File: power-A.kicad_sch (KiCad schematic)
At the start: 30 parts, among them J201 PCB Receptacle, J202 PCB Receptacle, J203 Conn_01x06, U201 AMS1117-ADJ_SOT223

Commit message: Ficup column name for JLCPCB/LCSC part no
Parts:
- C201: LCSC (none) -> C117040
- C203, C205: LCSC (none) -> C12891
- D201: LCSC (none) -> C78395
- D202, D203: LCSC (none) -> C12760
- D204, D205, D206: LCSC (none) -> C8598
- D207: LCSC (none) -> C2293
- R204, R210: LCSC (none) -> C25271
- U201: LCSC (none) -> C347224
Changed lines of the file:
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@@
+      (effects (font (size 1.27 1.27)) hide)
+    )
+    (property "LCSC" "C12760" (id 5) (at 68.58 93.98 0)
       (effects (font (size 1.27 1.27)) hide)
     )
@@
       (effects (font (size 1.27 1.27)) hide)
     )
+    (property "LCSC" "C25271" (id 5) (at 242.57 80.645 0)
+      (effects (font (size 1.27 1.27)) hide)
+    )
     (pin "1")
     (pin "2")
@@
       (effects (font (size 1.27 1.27)) hide)
     )
+    (property "LCSC" "C117040" (id 5) (at 139.7 91.44 0)
+      (effects (font (size 1.27 1.27)) hide)
+    )
     (pin "1")
     (pin "2")
@@
     )
     (property "JLCPCB" " C12891 " (id 4) (at 169.545 89.535 0)
+      (effects (font (size 1.27 1.27)) hide)
+    )
+    (property "LCSC" " C12891 " (id 5) (at 169.545 89.535 0)
       (effects (font (size 1.27 1.27)) hide)
     )
@@
       (effects (font (size 1.27 1.27)) hide)
     )
+    (property "LCSC" "C78395" (id 5) (at 60.325 91.44 0)
+      (effects (font (size 1.27 1.27)) hide)
+    )
     (pin "1")
     (pin "2")
@@
       (effects (font (size 1.27 1.27)) hide)
     )
+    (property "LCSC" "C347224" (id 5) (at 188.595 80.645 0)
+      (effects (font (size 1.27 1.27)) hide)
+    )
     (pin "1")
     (pin "2")
@@
     )
     (property "JLCPCB" "C8598 " (id 4) (at 190.5 138.43 0)
+      (effects (font (size 1.27 1.27)) hide)
+    )
+    (property "LCSC" "C8598 " (id 5) (at 190.5 138.43 0)
       (effects (font (size 1.27 1.27)) hide)
     )
@@
       (effects (font (size 1.27 1.27)) hide)
     )
+    (property "LCSC" "C25271" (id 5) (at 100.965 80.645 0)
+      (effects (font (size 1.27 1.27)) hide)
+    )
     (pin "1")
     (pin "2")
@@
     )
     (property "JLCPCB" "C12760" (id 4) (at 68.58 85.725 0)
+      (effects (font (size 1.27 1.27)) hide)
+    )
+    (property "LCSC" "C12760" (id 5) (at 68.58 85.725 0)
       (effects (font (size 1.27 1.27)) hide)
     )
@@
       (effects (font (size 1.27 1.27)) hide)
     )
+    (property "LCSC" "C8598 " (id 5) (at 190.5 128.27 0)
+      (effects (font (size 1.27 1.27)) hide)
+    )
     (pin "1")
     (pin "2")
@@
     )
     (property "JLCPCB" "C2293" (id 4) (at 255.27 92.075 0)
+      (effects (font (size 1.27 1.27)) hide)
+    )
+    (property "LCSC" "C2293" (id 5) (at 255.27 92.075 0)
       (effects (font (size 1.27 1.27)) hide)
     )
@@
       (effects (font (size 1.27 1.27)) hide)
     )
+    (property "LCSC" "C8598 " (id 5) (at 134.62 80.645 0)
+      (effects (font (size 1.27 1.27)) hide)
+    )
     (pin "1")
     (pin "2")
@@
       (effects (font (size 1.27 1.27)) hide)
     )
+    (property "LCSC" " C12891 " (id 5) (at 220.98 89.535 0)
+      (effects (font (size 1.27 1.27)) hide)
+    )

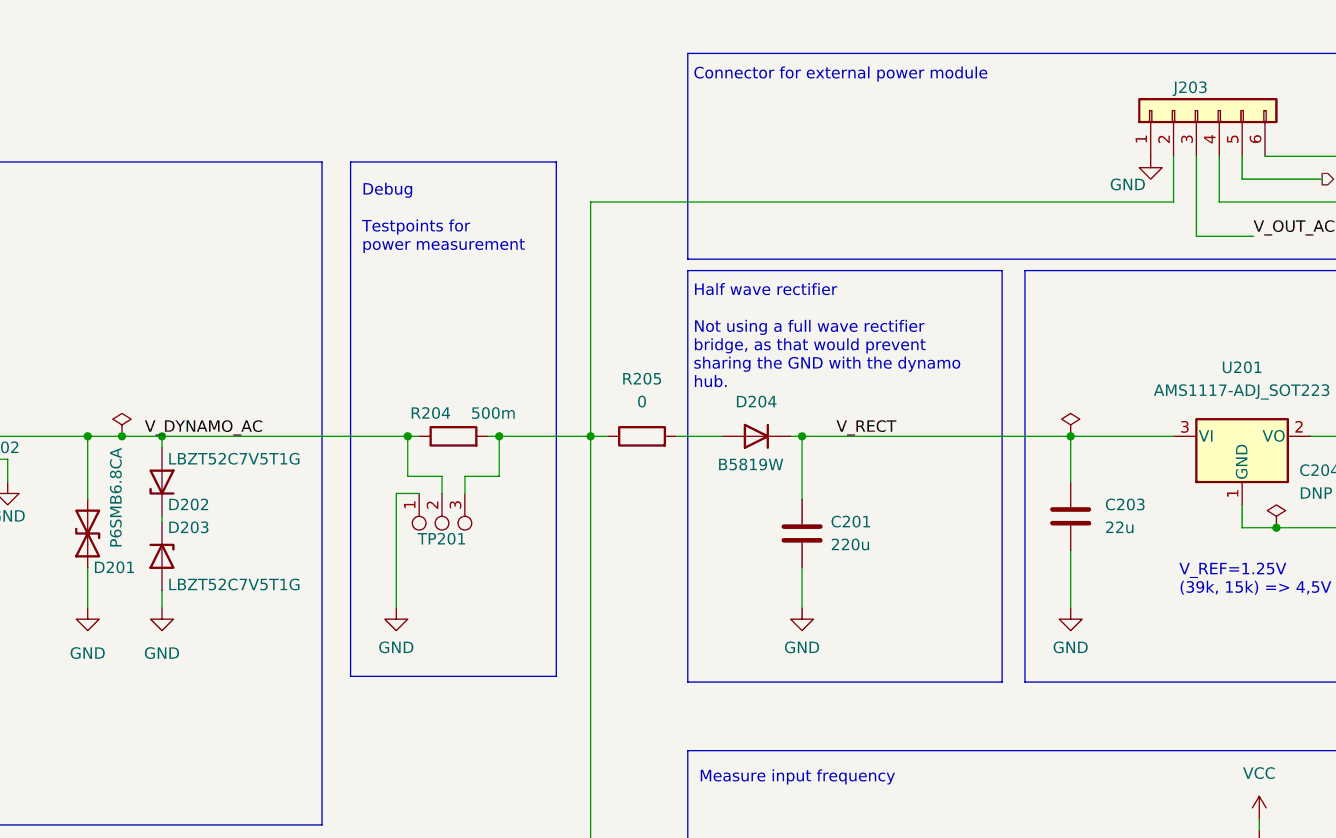
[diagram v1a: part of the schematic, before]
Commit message: move power module intput directly to V_DYNAMO_AC to ease routing
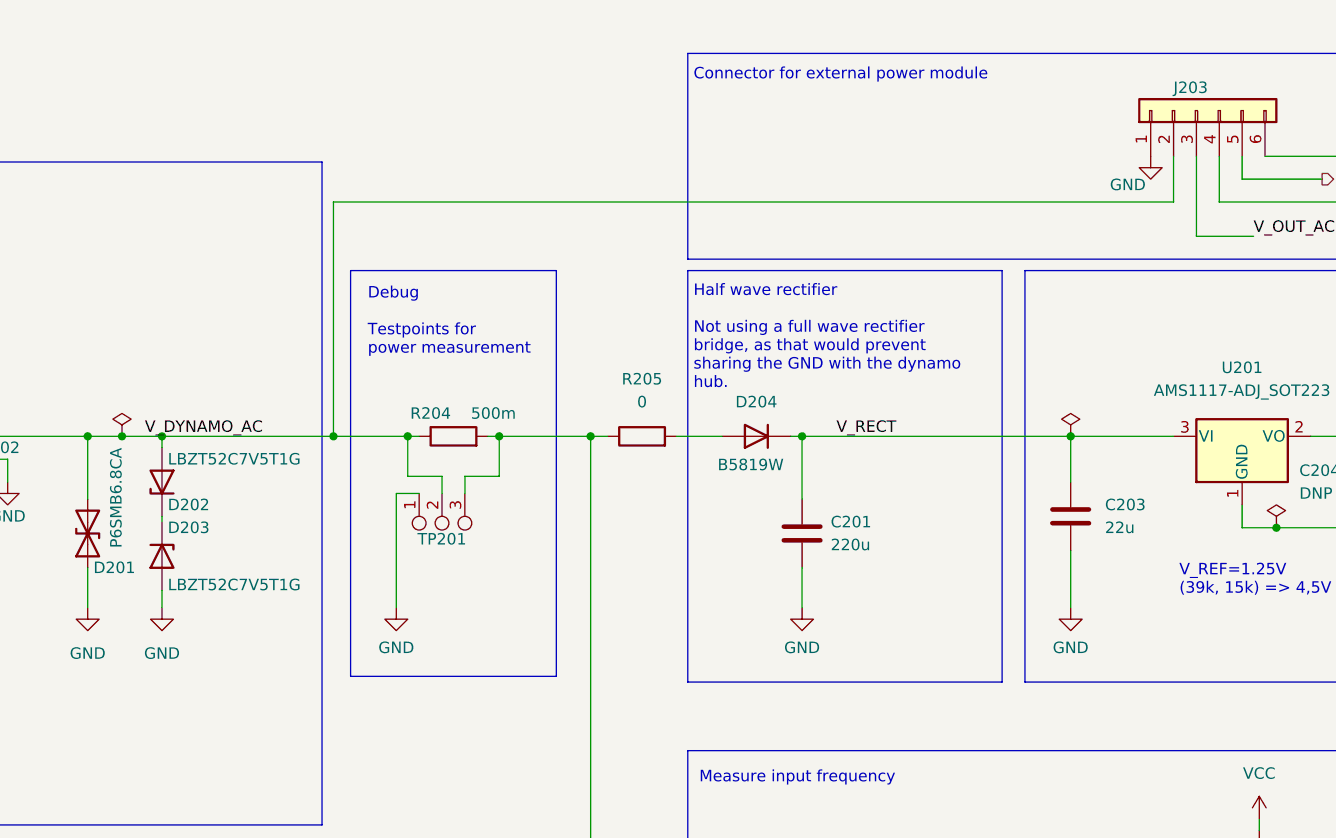
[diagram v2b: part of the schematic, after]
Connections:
- net V_DYNAMO_AC: now also J203.2 (Pin_2)
- net at R204.2, R205.1, R206.2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: no longer J203.2 (Pin_2)
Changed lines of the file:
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@@
     (comment 3 "CERN-OHL-S-2.0 https://spdx.org/licenses/CERN-OHL-S-2.0.html")
   )
+  (junction (at 87.63 80.645) (diameter 0) (color 0 0 0 0)
+  )
   (junction (at 95.885 80.645) (diameter 0) (color 0 0 0 0)
   )
@@
     (stroke (width 0) (type default) (color 0 0 0 0))
   )
-  (polyline (pts (xy 89.535 50.165) (xy 89.535 107.315))
+  (polyline (pts (xy 89.535 62.23) (xy 89.535 107.315))
     (stroke (width 0) (type default) (color 0 0 0 0))
   )
@@
     (stroke (width 0) (type default) (color 0 0 0 0))
   )
-  (polyline (pts (xy 112.395 50.165) (xy 112.395 107.315))
+  (polyline (pts (xy 112.395 62.23) (xy 112.395 107.315))
     (stroke (width 0) (type default) (color 0 0 0 0))
   )
@@
     (stroke (width 0) (type default) (color 0 0 0 0))
   )
+  (wire (pts (xy 87.63 80.645) (xy 95.885 80.645))
+    (stroke (width 0) (type default) (color 0 0 0 0))
+  )
   (wire (pts (xy 106.045 80.645) (xy 116.205 80.645))
     (stroke (width 0) (type default) (color 0 0 0 0))
@@
     (stroke (width 0) (type default) (color 0 0 0 0))
   )
-  (wire (pts (xy 116.205 80.645) (xy 116.205 54.61))
+  (wire (pts (xy 87.63 80.645) (xy 87.63 54.61))
     (stroke (width 0) (type default) (color 0 0 0 0))
   )
@@
     (stroke (width 0) (type default) (color 0 0 0 0))
   )
-  (wire (pts (xy 116.205 54.61) (xy 180.975 54.61))
+  (wire (pts (xy 87.63 54.61) (xy 180.975 54.61))
     (stroke (width 0) (type default) (color 0 0 0 0))
   )
@@
     (stroke (width 0) (type default) (color 0 0 0 0))
   )
-  (polyline (pts (xy 89.535 50.165) (xy 112.395 50.165))
+  (polyline (pts (xy 89.535 62.23) (xy 112.395 62.23))
     (stroke (width 0) (type default) (color 0 0 0 0))
   )
@@
     (stroke (width 0) (type default) (color 0 0 0 0))
   )
-  (wire (pts (xy 68.58 80.645) (xy 95.885 80.645))
+  (wire (pts (xy 68.58 80.645) (xy 87.63 80.645))
     (stroke (width 0) (type default) (color 0 0 0 0))
   )
@@
     (stroke (width 0) (type default) (color 0 0 0 0))
   )
-  (text "Debug\n\nTestpoints for\npower measurement" (at 90.805 60.325 0)
+  (text "Debug\n\nTestpoints for\npower measurement" (at 91.44 71.755 0)
     (effects (font (size 1.27 1.27)) (justify left bottom))
   )

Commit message: Mark some parts as 'exclude from bom'
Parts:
- D207: LCSC C2293 -> C72041
- TP201, TP202: value TestPoint_2Pole -> TestPoint_3Pole; now left out of the parts list
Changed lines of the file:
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@@
       (effects (font (size 1.27 1.27)) hide)
     )
-    (property "LCSC" "C2293" (id 5) (at 255.27 92.075 0)
+    (property "LCSC" "C72041" (id 5) (at 255.27 92.075 0)
       (effects (font (size 1.27 1.27)) hide)
     )
@@
   )
   (symbol (lib_id "project-lib:TestPoint_3Pole") (at 241.3 86.995 0) (unit 1)
-    (in_bom yes) (on_board yes)
+    (in_bom no) (on_board yes)
     (property "Reference" "TP202" (id 0) (at 241.3 92.075 0))
-    (property "Value" "TestPoint_2Pole" (id 1) (at 241.3 90.805 90)
+    (property "Value" "TestPoint_3Pole" (id 1) (at 241.3 90.805 90)
       (effects (font (size 1.27 1.27)) hide)
     )
@@
   )
   (symbol (lib_id "project-lib:TestPoint_3Pole") (at 99.695 86.995 0) (unit 1)
-    (in_bom yes) (on_board yes)
+    (in_bom no) (on_board yes)
     (property "Reference" "TP201" (id 0) (at 99.695 92.075 0))
-    (property "Value" "TestPoint_2Pole" (id 1) (at 99.695 90.805 90)
+    (property "Value" "TestPoint_3Pole" (id 1) (at 99.695 90.805 90)
       (effects (font (size 1.27 1.27)) hide)
     )

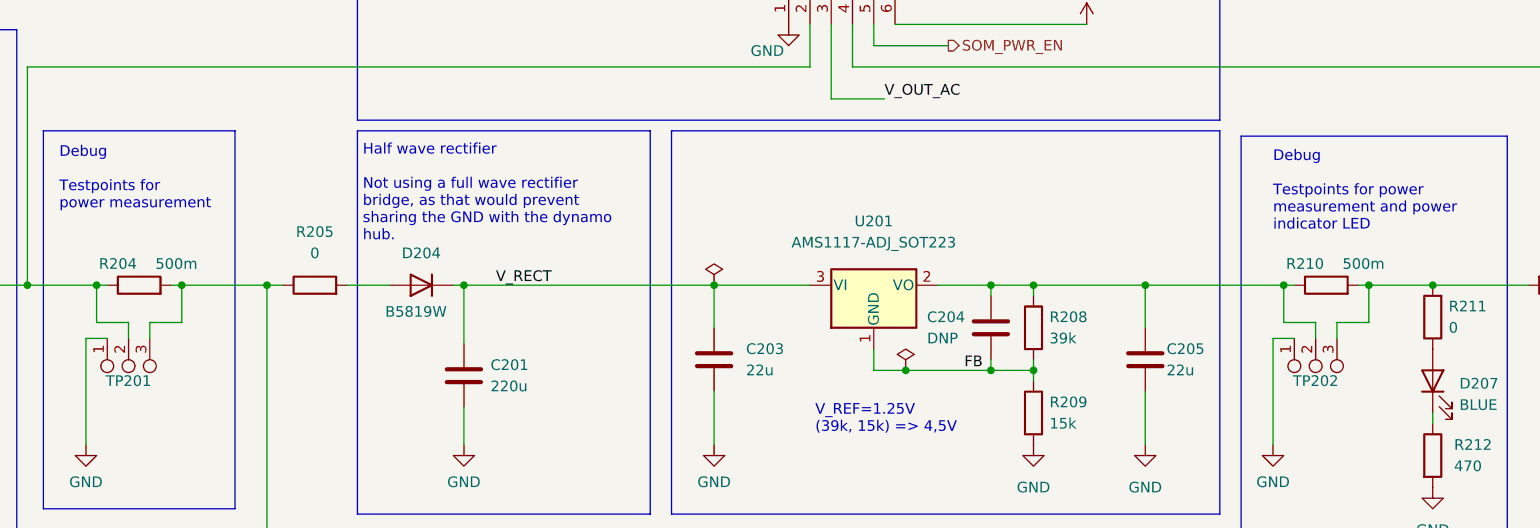
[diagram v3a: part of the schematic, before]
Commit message: Schematic: BOM consolidation and JLCPCB part no annotation
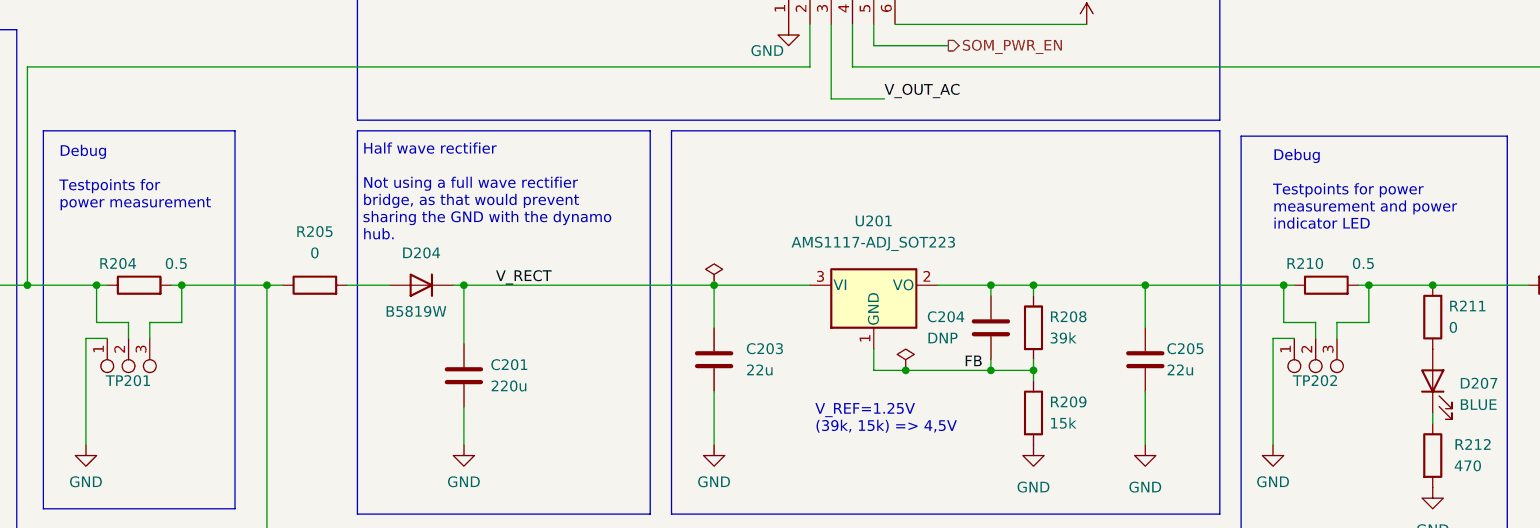
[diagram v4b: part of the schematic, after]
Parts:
- C202: LCSC (none) -> C57112
- C203, C205: LCSC C12891 -> C12891
- R201, R202, R205, R211, R213: LCSC (none) -> C17477
- R204, R210: value 500m -> 0.5; LCSC C25271 -> C28319
- R206: LCSC (none) -> C22961
- R207: LCSC (none) -> C25803
- R208: LCSC (none) -> C23153
- R209: LCSC (none) -> C22809
- R212: LCSC (none) -> C23179
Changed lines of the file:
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@@
+      (effects (font (size 1.27 1.27)) hide)
+    )
+    (property "LCSC" "C17477" (id 4) (at 33.655 99.06 0)
       (effects (font (size 1.27 1.27)) hide)
     )
@@
     (in_bom yes) (on_board yes)
     (property "Reference" "R210" (id 0) (at 240.03 78.105 90))
-    (property "Value" "500m" (id 1) (at 247.015 78.105 90))
+    (property "Value" "0.5" (id 1) (at 247.015 78.105 90))
     (property "Footprint" "Resistor_SMD:R_0805_2012Metric" (id 2) (at 242.57 82.423 90)
       (effects (font (size 1.27 1.27)) hide)
@@
       (effects (font (size 1.27 1.27)) hide)
     )
-    (property "LCSC" "C25271" (id 5) (at 242.57 80.645 0)
+    (property "LCSC" "C28319" (id 5) (at 242.57 80.645 0)
       (effects (font (size 1.27 1.27)) hide)
     )
@@
       (effects (font (size 1.27 1.27)) hide)
     )
-    (property "LCSC" " C12891 " (id 5) (at 169.545 89.535 0)
+    (property "LCSC" "C12891 " (id 5) (at 169.545 89.535 0)
       (effects (font (size 1.27 1.27)) hide)
     )
@@
       (effects (font (size 1.27 1.27)) hide)
     )
+    (property "LCSC" "C22809" (id 4) (at 207.645 95.885 0)
+      (effects (font (size 1.27 1.27)) hide)
+    )
     (pin "1")
     (pin "2")
@@
     )
     (property "Datasheet" "~" (id 3) (at 255.27 84.455 0)
+      (effects (font (size 1.27 1.27)) hide)
+    )
+    (property "LCSC" "C17477" (id 4) (at 255.27 84.455 0)
       (effects (font (size 1.27 1.27)) hide)
     )
@@
       (effects (font (size 1.27 1.27)) hide)
     )
+    (property "LCSC" "C22961" (id 4) (at 137.16 133.35 0)
+      (effects (font (size 1.27 1.27)) hide)
+    )
     (pin "1")
     (pin "2")
@@
     )
     (property "Datasheet" "~" (id 3) (at 158.75 138.557 0)
+      (effects (font (size 1.27 1.27)) hide)
+    )
+    (property "LCSC" "C25803" (id 4) (at 158.75 138.557 0)
       (effects (font (size 1.27 1.27)) hide)
     )
@@
       (effects (font (size 1.27 1.27)) hide)
     )
+    (property "LCSC" "C17477" (id 4) (at 45.72 83.185 0)
+      (effects (font (size 1.27 1.27)) hide)
+    )
     (pin "1")
     (pin "2")
@@
     )
     (property "Datasheet" "~" (id 3) (at 255.27 100.965 0)
+      (effects (font (size 1.27 1.27)) hide)
+    )
+    (property "LCSC" "C23179" (id 4) (at 255.27 100.965 0)
       (effects (font (size 1.27 1.27)) hide)
     )
@@
     )
     (property "Datasheet" "~" (id 3) (at 270.51 80.645 0)
+      (effects (font (size 1.27 1.27)) hide)
+    )
+    (property "LCSC" "C17477" (id 4) (at 270.51 80.645 0)
       (effects (font (size 1.27 1.27)) hide)
     )
@@
     (in_bom yes) (on_board yes)
     (property "Reference" "R204" (id 0) (at 98.425 78.105 90))
-    (property "Value" "500m" (id 1) (at 105.41 78.105 90))
+    (property "Value" "0.5" (id 1) (at 105.41 78.105 90))
     (property "Footprint" "Resistor_SMD:R_0805_2012Metric" (id 2) (at 100.965 82.423 90)
       (effects (font (size 1.27 1.27)) hide)
@@
       (effects (font (size 1.27 1.27)) hide)
     )
-    (property "LCSC" "C25271" (id 5) (at 100.965 80.645 0)
+    (property "LCSC" "C28319" (id 5) (at 100.965 80.645 0)
       (effects (font (size 1.27 1.27)) hide)
     )
@@
     )
     (property "Datasheet" "~" (id 3) (at 207.645 85.725 0)
+      (effects (font (size 1.27 1.27)) hide)
+    )
+    (property "LCSC" "C23153" (id 4) (at 207.645 85.725 0)
       (effects (font (size 1.27 1.27)) hide)
     )
@@
       (effects (font (size 1.27 1.27)) hide)
     )
-    (property "LCSC" " C12891 " (id 5) (at 220.98 89.535 0)
+    (property "LCSC" "C12891 " (id 5) (at 220.98 89.535 0)
       (effects (font (size 1.27 1.27)) hide)
     )
@@
       (effects (font (size 1.27 1.27)) hide)
     )
+    (property "LCSC" "C17477" (id 4) (at 121.92 80.645 0)
+      (effects (font (size 1.27 1.27)) hide)
+    )
     (pin "1")
     (pin "2")
@@
       (effects (font (size 1.27 1.27)) hide)
     )
+    (property "LCSC" "C57112" (id 4) (at 163.83 138.43 0)
+      (effects (font (size 1.27 1.27)) hide)
+    )
